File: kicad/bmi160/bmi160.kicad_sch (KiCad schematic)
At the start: 39 parts, among them J1 USB4125-GF-A_REVA, J2 Conn_02x03_Odd_Even, J3 Conn_01x05, J4 Conn_01x02, SW1 SW_SPDT, U1 MCP73832-2-OT, U2 BQ297xy, U3 CSD85302L, U4 NCP177BMX330TCG, U5 ASAK-32.7680KHZ-LRS-T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

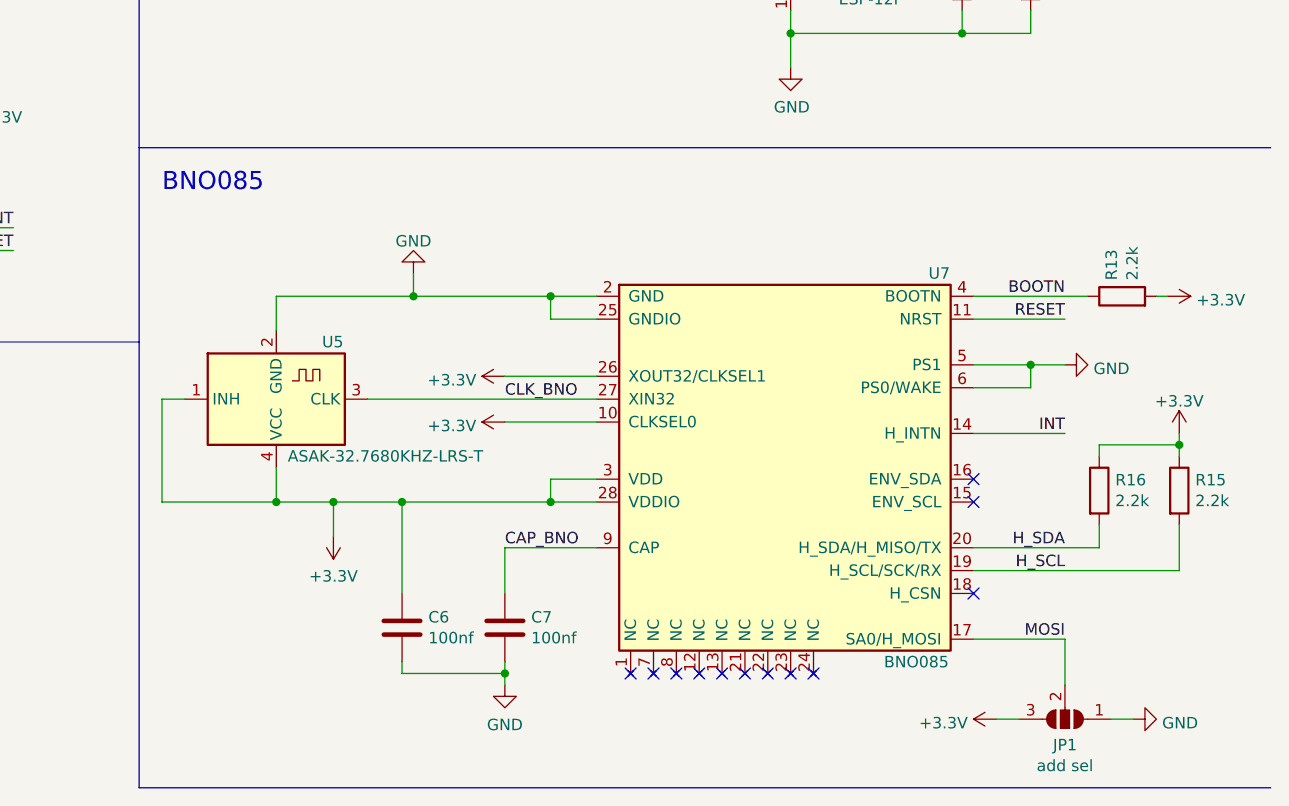
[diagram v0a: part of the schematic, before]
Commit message: added basic support for bmi160, it shold work i haven had a chance to test thogh
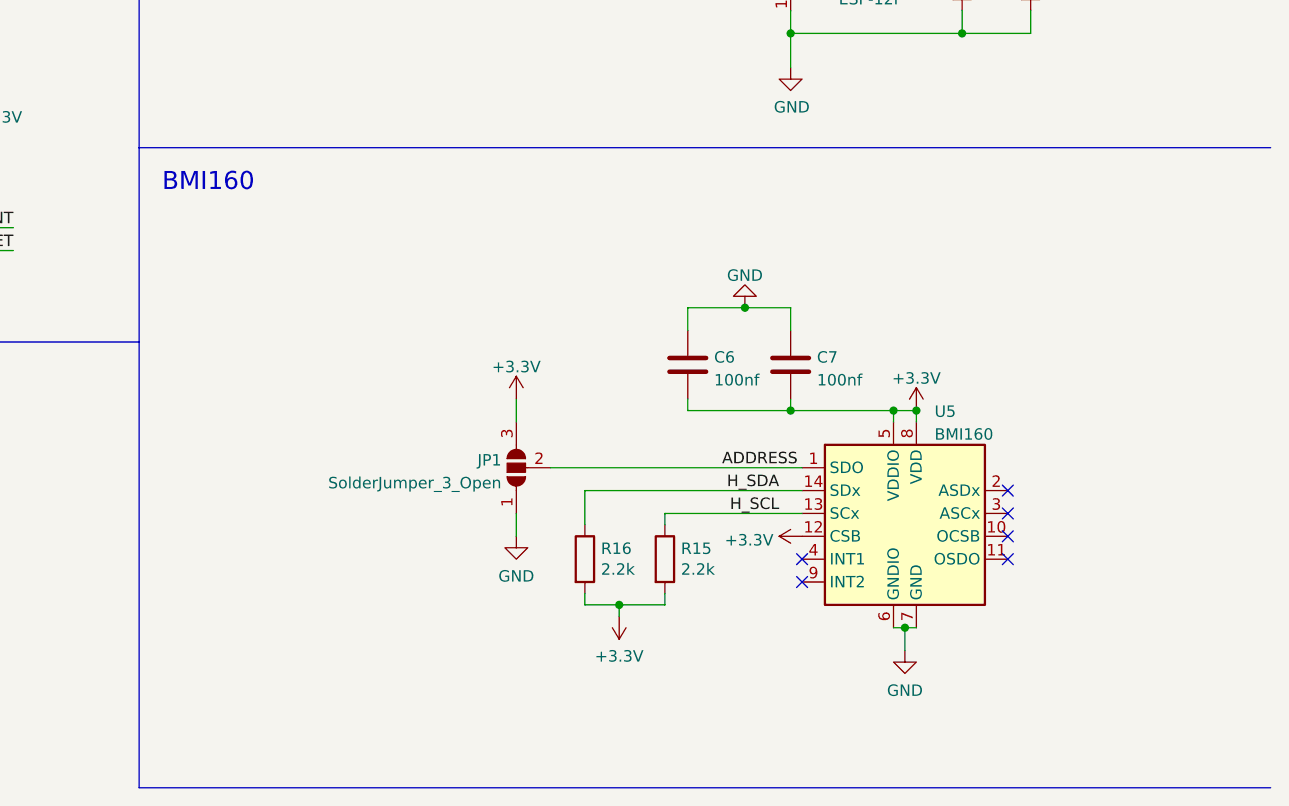
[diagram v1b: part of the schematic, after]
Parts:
- removed JP1: add sel, Jumper:SolderJumper-3_P2.0mm_Open_TrianglePad1.0x1.5mm, symbol slime-rescue:SolderJumper_3_Open-Jumper
- removed R13: 2.2k, Resistor_SMD:R_0402_1005Metric, symbol Device:R
- removed U5: ASAK-32.7680KHZ-LRS-T, Oscillator:kc2016, symbol slime-rescue:KC2520Z-Oscillator
- removed U7: BNO085, Package_LGA:LGA-28_5.2x3.8mm_P0.5mm, symbol slime-rescue:BNO085-Sensor
- added JP1: SolderJumper_3_Open, Jumper:SolderJumper-3_P2.0mm_Open_TrianglePad1.0x1.5mm, symbol Jumper:SolderJumper_3_Open
- added U5: BMI160, Package_LGA:Bosch_LGA-14_3x2.5mm_P0.5mm, symbol Sensor_Motion:BMI160
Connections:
- net CAP_BNO is gone; now on net GND: C7.1
- net +3.3V: now also C6.2, C7.2, R15.2, R16.2, JP1.3 (B), U5.12 (CSB), U5.5 (VDDIO), U5.8 (VDD); no longer C6.1, R15.1, R16.1
- net GND: now also C6.1, JP1.1 (A), U5.6 (GNDIO), U5.7 (GND); no longer C6.2, C7.2
- net H_SCL: now also R15.1, U5.13 (SCx); no longer R15.2
- net H_SDA: now also R16.1, U5.14 (SDx); no longer R16.2
- new net ADDRESS: JP1.2 (C), U5.1 (SDO)
- no-connect marks 20 -> 14
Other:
- note added: "BMI160"
- note removed: "BNO085"
- title: slime_minimax with bno085 -> slime_minimax with bmi160
- moved on the sheet: R15, R16
